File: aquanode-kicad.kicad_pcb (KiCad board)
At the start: 2 copper layers, 1 part

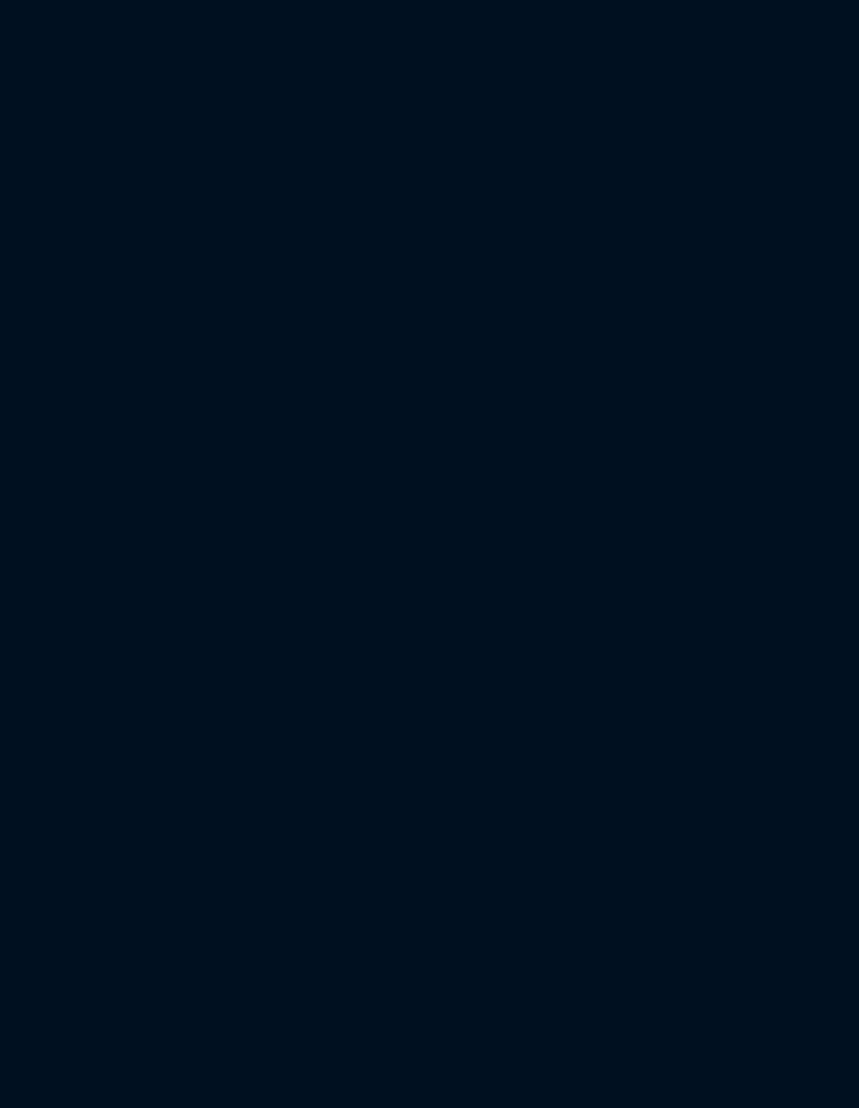
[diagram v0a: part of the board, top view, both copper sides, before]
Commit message: asignar huellas
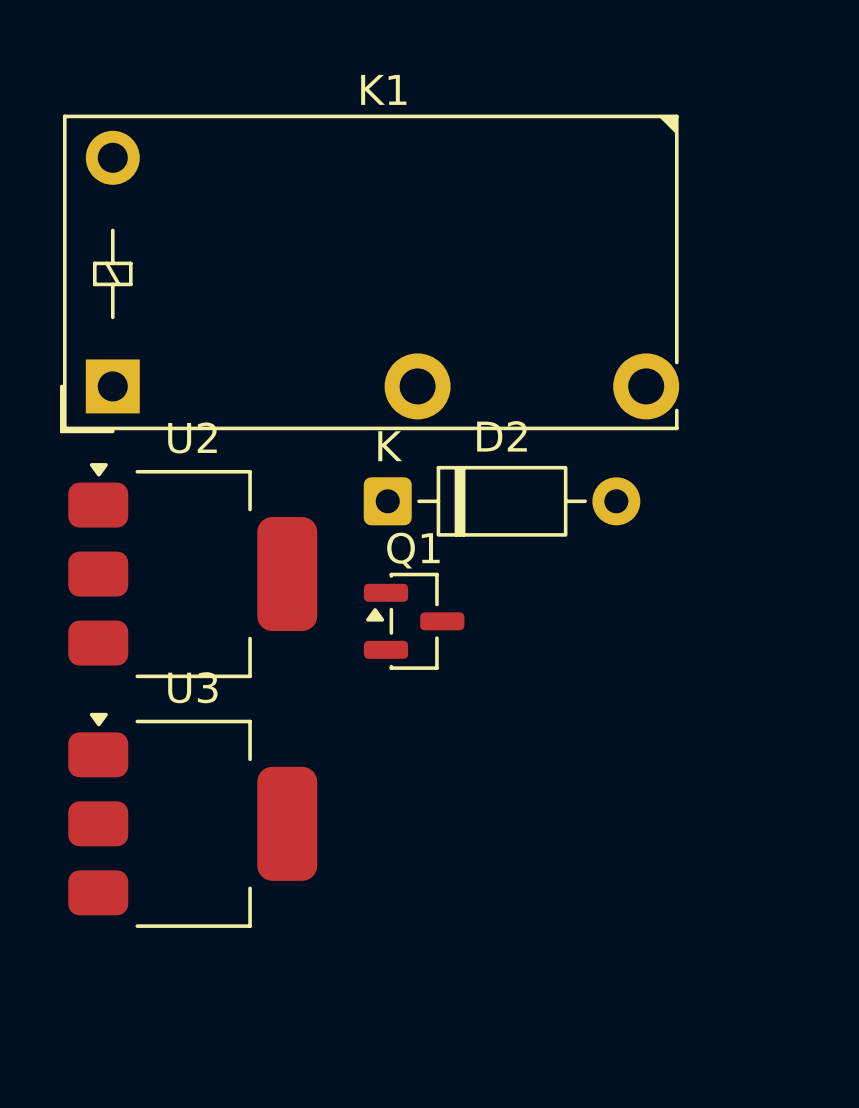
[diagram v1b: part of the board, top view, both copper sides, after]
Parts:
- added D2: 1N4148, Diode_THT:D_DO-35_SOD27_P7.62mm_Horizontal, F.Cu at (10.9, 12.9)
- added K1: RM50-xx21, Relay_THT:Relay_SPST_Finder_32.21-x300, F.Cu at (1.76, 9.07)
- added Q1: BC817, Package_TO_SOT_SMD:SOT-23, F.Cu at (11.8, 16.9)
- added U2: AMS1117-3.3, Package_TO_SOT_SMD:SOT-223-3_TabPin2, F.Cu at (4.42, 15.3)
- added U3: AMS1117-5.0, Package_TO_SOT_SMD:SOT-223-3_TabPin2, F.Cu at (4.42, 23.7)
